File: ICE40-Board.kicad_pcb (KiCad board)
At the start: 4 copper layers, 134.4 x 58 mm, 82 parts, among them SW1 SW_Push, U1 ADP1712AUJZ-3.3, U10 FT4222HQ, U11 74LS125, U12 74LS126, U2 ADP1712AUJZ-2.5, U3 ADP1712AUJZ-1.2, U4 Barrel_Jack, U5 W25X20CLSNIG, U6 USB_C_Receptacle_USB2.0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

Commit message: Minor changed
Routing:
- net Net-(U7-Pad42): track 33.5 -> 31.1 mm
- net Net-(U7-Pad43): track 32.1 -> 30.0 mm
- net Net-(U7-Pad44): track 39.0 -> 37.3 mm
- net Net-(U7-Pad45): track 43.6 -> 42.3 mm
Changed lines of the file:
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@@
   (gr_line (start 22.987 74.676) (end 152.908 74.676) (layer "Edge.Cuts") (width 0.1))
   (gr_arc (start 20.701 18.796) (mid 21.333356 17.269356) (end 22.86 16.637) (layer "Edge.Cuts") (width 0.1))
-  (segment (start 101.9355 40.4675) (end 116.205 40.4675) (width 0.2) (layer "F.Cu") (net 1))
-  (segment (start 98.552 39.624) (end 101.092 39.624) (width 0.2) (layer "F.Cu") (net 1))
-  (segment (start 94.234 46.99) (end 97.79 43.434) (width 0.2) (layer "F.Cu") (net 1))
-  (segment (start 94.291006 51.308) (end 95.14152 50.457486) (width 0.2) (layer "F.Cu") (net 1))
-  (segment (start 89.916 56.896) (end 90.678 56.896) (width 0.2) (layer "F.Cu") (net 1))
-  (segment (start 94.234 48.006) (end 94.234 46.99) (width 0.2) (layer "F.Cu") (net 1))
-  (segment (start 95.14152 48.91352) (end 94.234 48.006) (width 0.2) (layer "F.Cu") (net 1))
-  (segment (start 97.79 40.386) (end 98.552 39.624) (width 0.2) (layer "F.Cu") (net 1))
+  (segment (start 97.917 43.688) (end 97.917 41.402) (width 0.2) (layer "F.Cu") (net 1))
+  (segment (start 90.678 56.896) (end 91.44848 56.12552) (width 0.2) (layer "F.Cu") (net 1))
   (segment (start 92.964 51.308) (end 94.291006 51.308) (width 0.2) (layer "F.Cu") (net 1))
   (segment (start 95.14152 50.457486) (end 95.14152 48.91352) (width 0.2) (layer "F.Cu") (net 1))
+  (segment (start 91.44848 52.82352) (end 92.964 51.308) (width 0.2) (layer "F.Cu") (net 1))
+  (segment (start 89.535 56.515) (end 89.916 56.896) (width 0.2) (layer "F.Cu") (net 1))
+  (segment (start 115.356349 40.386) (end 115.437849 40.4675) (width 0.2) (layer "F.Cu") (net 1))
+  (segment (start 94.234 48.006) (end 94.234 47.371) (width 0.2) (layer "F.Cu") (net 1))
+  (segment (start 97.917 41.402) (end 98.933 40.386) (width 0.2) (layer "F.Cu") (net 1))
+  (segment (start 115.437849 40.4675) (end 116.205 40.4675) (width 0.2) (layer "F.Cu") (net 1))
+  (segment (start 94.291006 51.308) (end 95.14152 50.457486) (width 0.2) (layer "F.Cu") (net 1))
   (segment (start 89.535 54.291) (end 89.535 56.515) (width 0.2) (layer "F.Cu") (net 1))
-  (segment (start 89.535 56.515) (end 89.916 56.896) (width 0.2) (layer "F.Cu") (net 1))
-  (segment (start 90.678 56.896) (end 91.44848 56.12552) (width 0.2) (layer "F.Cu") (net 1))
-  (segment (start 91.44848 52.82352) (end 92.964 51.308) (width 0.2) (layer "F.Cu") (net 1))
+  (segment (start 98.933 40.386) (end 115.356349 40.386) (width 0.2) (layer "F.Cu") (net 1))
+  (segment (start 94.234 47.371) (end 97.917 43.688) (width 0.2) (layer "F.Cu") (net 1))
   (segment (start 91.44848 56.12552) (end 91.44848 52.82352) (width 0.2) (layer "F.Cu") (net 1))
-  (segment (start 97.79 43.434) (end 97.79 40.386) (width 0.2) (layer "F.Cu") (net 1))
-  (segment (start 101.092 39.624) (end 101.9355 40.4675) (width 0.2) (layer "F.Cu") (net 1))
-  (segment (start 97.17352 40.24048) (end 98.806 38.608) (width 0.2) (layer "F.Cu") (net 2))
-  (segment (start 102.845488 39.9675) (end 116.205 39.9675) (width 0.2) (layer "F.Cu") (net 2))
+  (segment (start 89.916 56.896) (end 90.678 56.896) (width 0.2) (layer "F.Cu") (net 1))
+  (segment (start 95.14152 48.91352) (end 94.234 48.006) (width 0.2) (layer "F.Cu") (net 1))
+  (segment (start 97.17352 41.25648) (end 98.4625 39.9675) (width 0.2) (layer "F.Cu") (net 2))
+  (segment (start 90.805 54.291) (end 90.805 52.197) (width 0.2) (layer "F.Cu") (net 2))
   (segment (start 94.742 50.292) (end 94.742 49.127283) (width 0.2) (layer "F.Cu") (net 2))
-  (segment (start 101.485988 38.608) (end 102.845488 39.9675) (width 0.2) (layer "F.Cu") (net 2))
-  (segment (start 93.74452 48.129803) (end 93.74452 46.802989) (width 0.2) (layer "F.Cu") (net 2))
-  (segment (start 98.806 38.608) (end 101.485988 38.608) (width 0.2) (layer "F.Cu") (net 2))
   (segment (start 94.234 50.8) (end 94.742 50.292) (width 0.2) (layer "F.Cu") (net 2))
-  (segment (start 93.74452 46.802989) (end 97.17352 43.373989) (width 0.2) (layer "F.Cu") (net 2))
+  (segment (start 93.74452 47.09848) (end 97.17352 43.66948) (width 0.2) (layer "F.Cu") (net 2))
+  (segment (start 90.805 52.197) (end 92.202 50.8) (width 0.2) (layer "F.Cu") (net 2))
+  (segment (start 93.74452 48.129803) (end 93.74452 47.09848) (width 0.2) (layer "F.Cu") (net 2))
+  (segment (start 92.202 50.8) (end 94.234 50.8) (width 0.2) (layer "F.Cu") (net 2))
+  (segment (start 98.4625 39.9675) (end 116.205 39.9675) (width 0.2) (layer "F.Cu") (net 2))
+  (segment (start 97.17352 43.66948) (end 97.17352 41.25648) (width 0.2) (layer "F.Cu") (net 2))
   (segment (start 94.742 49.127283) (end 93.74452 48.129803) (width 0.2) (layer "F.Cu") (net 2))
-  (segment (start 90.805 54.291) (end 90.805 52.197) (width 0.2) (layer "F.Cu") (net 2))
-  (segment (start 90.805 52.197) (end 92.202 50.8) (width 0.2) (layer "F.Cu") (net 2))
-  (segment (start 92.202 50.8) (end 94.234 50.8) (width 0.2) (layer "F.Cu") (net 2))
-  (segment (start 97.17352 43.373989) (end 97.17352 40.24048) (width 0.2) (layer "F.Cu") (net 2))
   (segment (start 102.7665 56.134) (end 104.648 56.134) (width 0.4) (layer "F.Cu") (net 3))
   (segment (start 126.1175 58.2865) (end 126.1175 55.88) (width 0.2) (layer "F.Cu") (net 3))
@@
   (segment (start 107.442 42.418) (end 107.442 41.0475) (width 0.2) (layer "B.Cu") (net 4))
   (segment (start 107.188 48.387) (end 107.0875 48.2865) (width 0.2) (layer "B.Cu") (net 4))
-  (segment (start 101.288994 37.846) (end 102.910494 39.4675) (width 0.2) (layer "F.Cu") (net 5))
-  (segment (start 98.298 37.846) (end 101.288994 37.846) (width 0.2) (layer "F.Cu") (net 5))
-  (segment (start 96.774 39.37) (end 98.298 37.846) (width 0.2) (layer "F.Cu") (net 5))
-  (segment (start 93.345 46.637503) (end 96.774 43.208503) (width 0.2) (layer "F.Cu") (net 5))
-  (segment (start 102.910494 39.4675) (end 116.205 39.4675) (width 0.2) (layer "F.Cu") (net 5))
-  (segment (start 93.345 49.341) (end 93.345 46.637503) (width 0.2) (layer "F.Cu") (net 5))
-  (segment (start 96.774 43.208503) (end 96.774 39.37) (width 0.2) (layer "F.Cu") (net 5))
-  (segment (start 101.346 37.338) (end 102.9755 38.9675) (width 0.2) (layer "F.Cu") (net 6))
-  (segment (start 92.075 47.117) (end 96.012 43.18) (width 0.2) (layer "F.Cu") (net 6))
-  (segment (start 102.9755 38.9675) (end 116.205 38.9675) (width 0.2) (layer "F.Cu") (net 6))
-  (segment (start 96.012 43.18) (end 96.012 39.116) (width 0.2) (layer "F.Cu") (net 6))
-  (segment (start 92.075 49.341) (end 92.075 47.117) (width 0.2) (layer "F.Cu") (net 6))
-  (segment (start 96.012 39.116) (end 97.79 37.338) (width 0.2) (layer "F.Cu") (net 6))
-  (segment (start 97.79 37.338) (end 101.346 37.338) (width 0.2) (layer "F.Cu") (net 6))
+  (segment (start 93.345 46.355) (end 96.647 43.053) (width 0.2) (layer "F.Cu") (net 5))
+  (segment (start 96.647 43.053) (end 96.647 40.894) (width 0.2) (layer "F.Cu") (net 5))
+  (segment (start 93.345 49.341) (end 93.345 46.355) (width 0.2) (layer "F.Cu") (net 5))
+  (segment (start 96.647 40.894) (end 98.0735 39.4675) (width 0.2) (layer "F.Cu") (net 5))
+  (segment (start 98.0735 39.4675) (end 116.205 39.4675) (width 0.2) (layer "F.Cu") (net 5))
+  (segment (start 92.075 46.736) (end 96.012 42.799) (width 0.2) (layer "F.Cu") (net 6))
+  (segment (start 96.012 42.799) (end 96.012 40.767) (width 0.2) (layer "F.Cu") (net 6))
+  (segment (start 92.075 49.341) (end 92.075 46.736) (width 0.2) (layer "F.Cu") (net 6))
+  (segment (start 96.012 40.767) (end 97.8115 38.9675) (width 0.2) (layer "F.Cu") (net 6))
+  (segment (start 97.8115 38.9675) (end 116.205 38.9675) (width 0.2) (layer "F.Cu") (net 6))
   (segment (start 97.282 36.576) (end 102.698982 36.576) (width 0.2) (layer "F.Cu") (net 7))
   (segment (start 102.698982 36.576) (end 104.590482 38.4675) (width 0.2) (layer "F.Cu") (net 7))

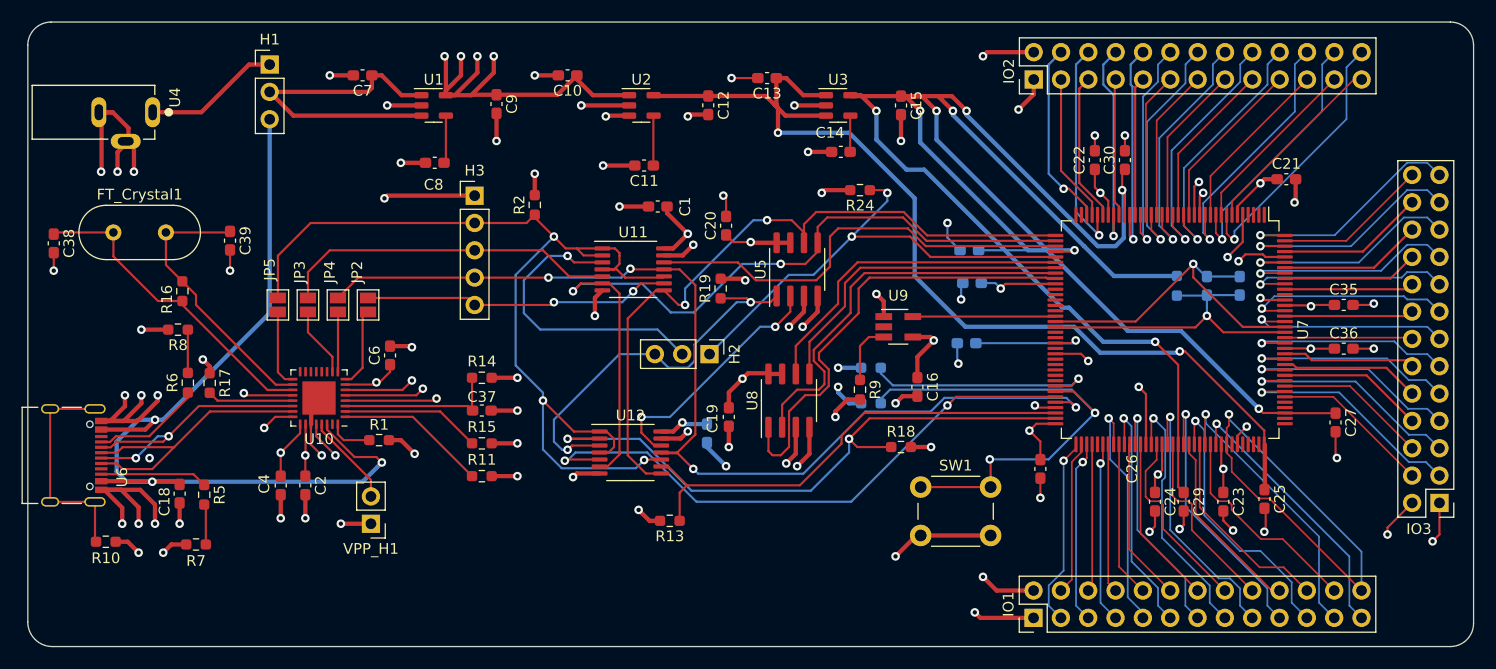
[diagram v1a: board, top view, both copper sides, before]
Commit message: Adjusted component and track clearances
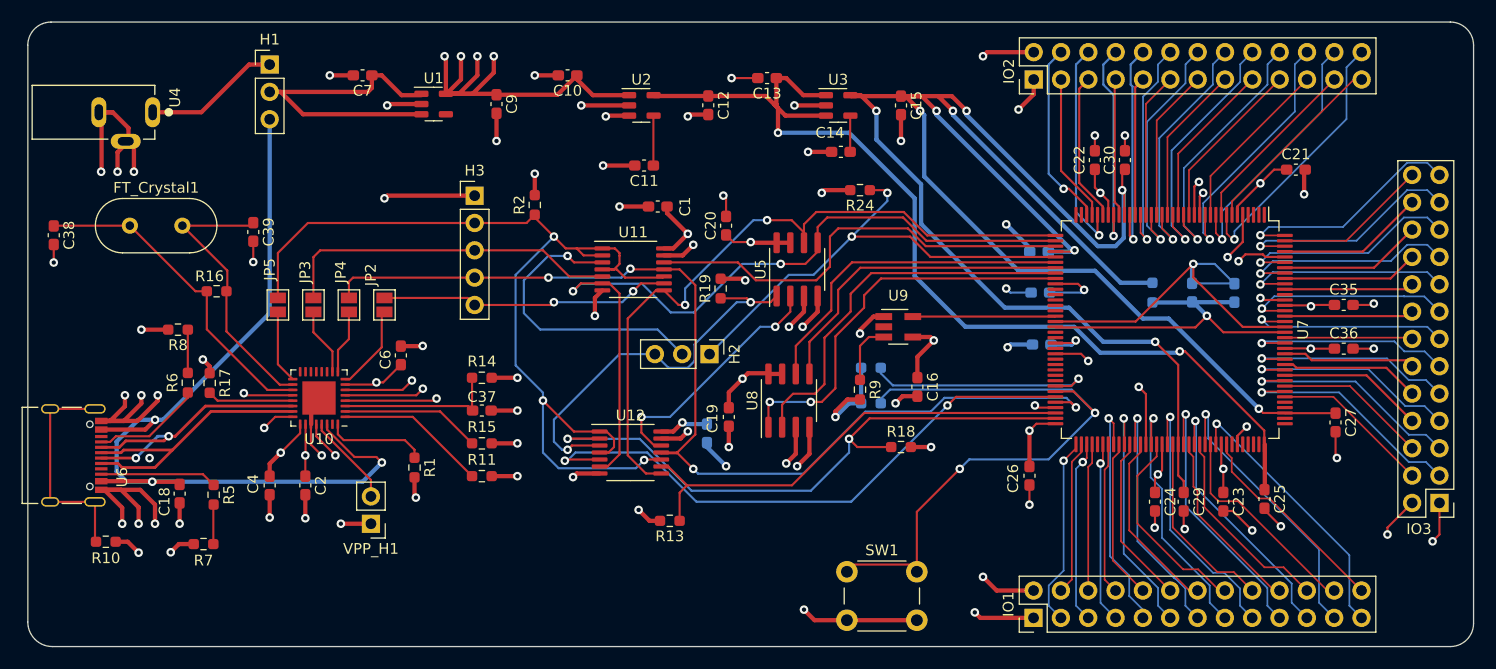
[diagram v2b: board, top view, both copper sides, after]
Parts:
- removed C8: 10nF, Capacitor_SMD:C_0603_1608Metric_Pad1.08x0.95mm_HandSolder
- IO3: value Conn_02x13_Row_Letter_Last -> Conn_02x09_Row_Letter_Last
- U1: value ADP1712AUJZ-3.3 -> ADP122AUJZ-3.3-R7
- moved SW1 10.4 mm to (96.8, 67.7)
- moved C31 6.99 mm to (114.9, 46.6)
- moved C28 6.48 mm to (114.7, 38.0)
- moved C32 6.41 mm to (114.8, 41.8)
- moved R1 4.16 mm to (56.6, 58.0), turned to -90 degrees
- moved R16 3.19 mm to (38.3, 41.7), turned to 0 degrees
- moved R12 2.36 mm to (125.2, 41.8)
- moved C39 2.30 mm to (41.7, 36.1)
- moved FT_Crystal1 1.66 mm to (30.2, 35.6)
- moved JP2 1.52 mm to (53.8, 42.9)
- moved C34 1.52 mm to (128.9, 41.8)
- moved C21 1.26 mm to (138.6, 30.4)
- moved C26 1.20 mm to (113.8, 58.8)
- moved C4 1.03 mm to (43.2, 59.7)
- moved JP4 1.02 mm to (50.5, 42.9)
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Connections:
- U1 pad 4: Net-(C8-Pad1) -> unconnected-(U1-Pad4)
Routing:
- net /12b: track 43.7 -> 19.4 mm, vias 1 -> 0
- net Net-(R4-Pad1): track 46.8 -> 58.5 mm
- net +1V2: track 213.2 -> 207.2 mm
- net /GND_PLL1: track 31.5 -> 37.1 mm
- net Net-(R1-Pad1): track 4.08 -> 9.39 mm
- net Net-(U7-Pad45): track 42.3 -> 37.2 mm, vias 0 -> 2
- net Net-(C8-Pad1): track 4.46 -> 0.00 mm
- net GND: track 251.2 -> 253.3 mm, vias 78 -> 77
- net +3V3: track 206.7 -> 204.7 mm, vias 42 -> 40
- net /VCC_PLL1: track 30.1 -> 31.9 mm
- net /SCK_EXT: track 28.6 -> 27.1 mm
- net /6b: track 15.8 -> 17.1 mm
- net /7b: track 17.6 -> 18.8 mm
- net Net-(U7-Pad44): track 37.3 -> 36.1 mm
- net /10a: track 25.9 -> 24.8 mm
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
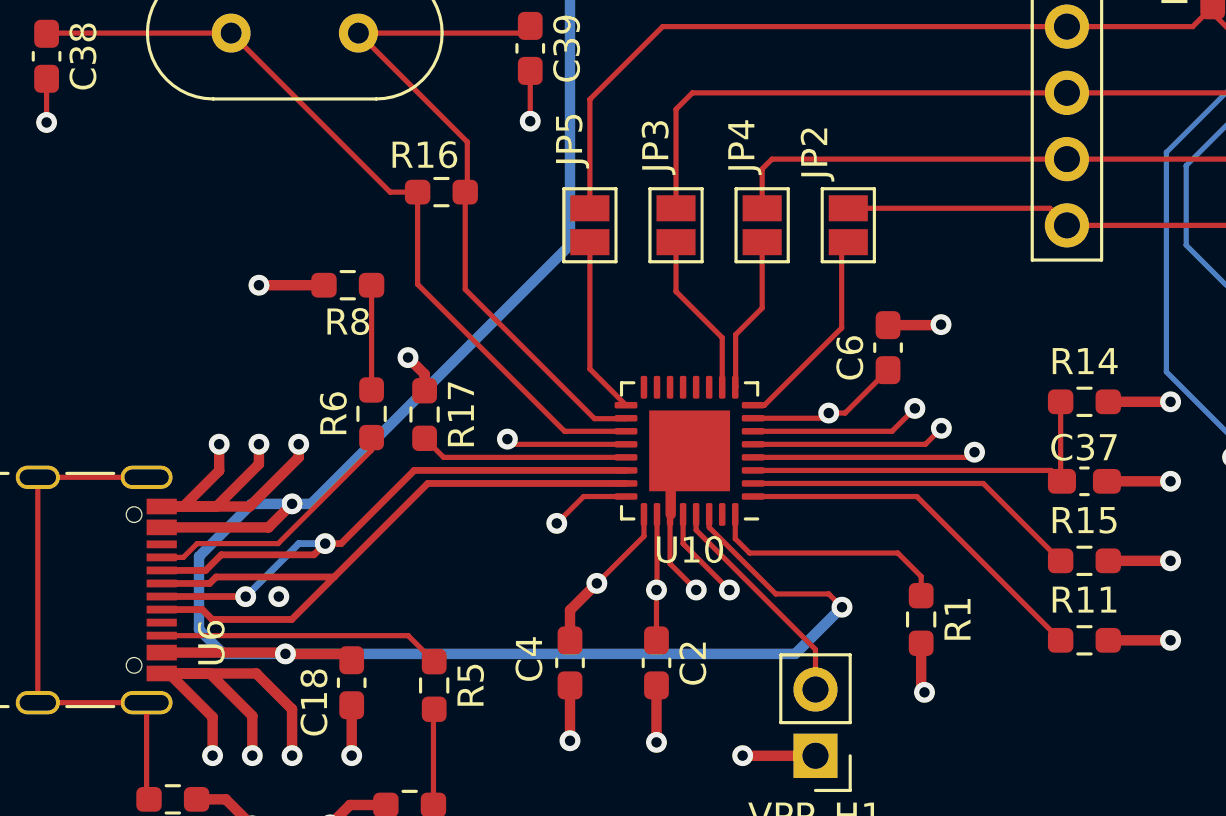
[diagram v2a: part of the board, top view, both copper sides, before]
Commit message: Impedance controlled USB routing
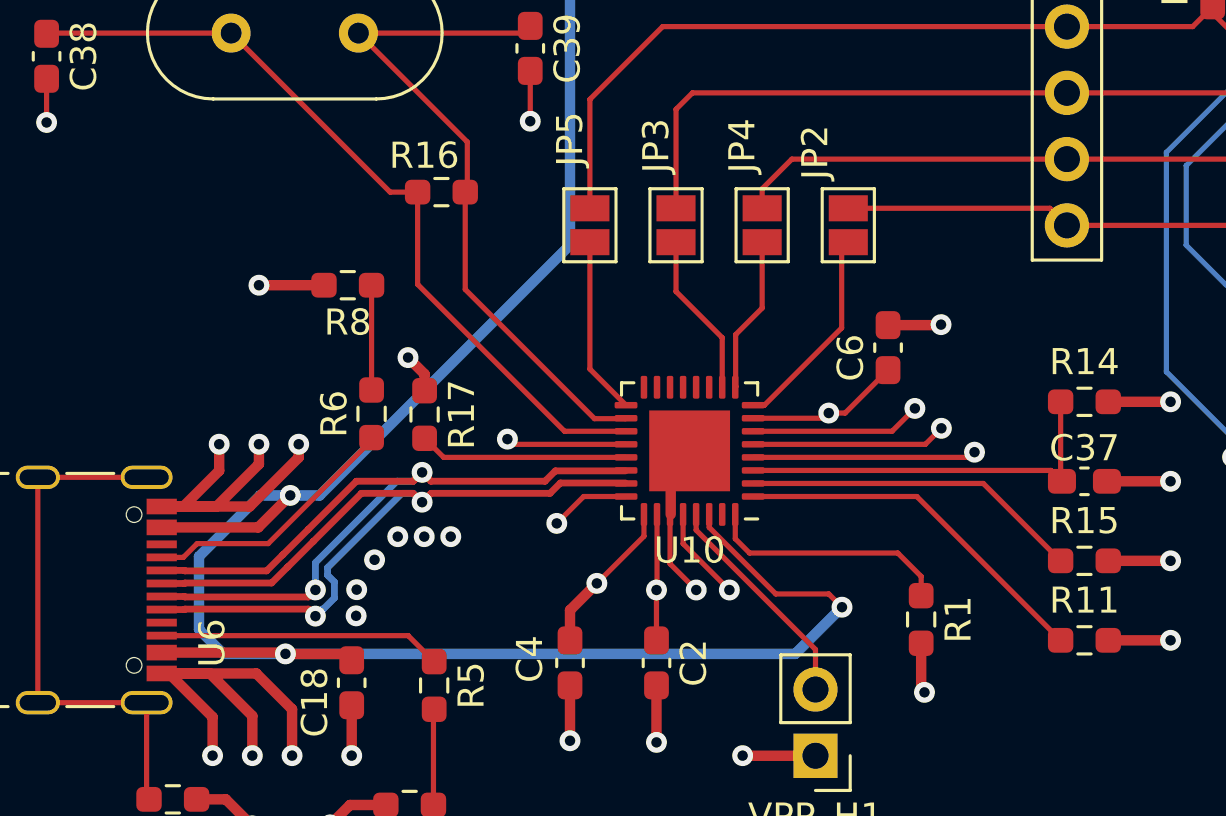
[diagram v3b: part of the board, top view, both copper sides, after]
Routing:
- net D+: track 26.8 -> 32.9 mm, vias 0 -> 2
- net D-: track 26.5 -> 32.2 mm
- net GND: vias 77 -> 82

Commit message: Added ground vias for better signal integrity, added silkscreen text, added reset button for MCU
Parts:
- added R20: 10k, Resistor_SMD:R_0603_1608Metric_Pad0.98x0.95mm_HandSolder, F.Cu at (72.0, 68.6)
- added SW2: SW_Push, Button_Switch_THT:SW_PUSH_6mm, F.Cu at (79.0, 67.7)
- R3, R4: moved to F.Cu
- moved R4 17.7 mm to (91.1, 67.8), turned to -90 degrees
- moved R3 10.3 mm to (109.3, 48.9)
- moved VPP_H1 3.92 mm to (52.6, 67.2)
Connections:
- IO3 pad 1: +3V3 -> GND
- IO3 pad 2: GND -> +3V3
- U7 pad 110: unconnected-(U7-Pad110) -> /MCU_RESET
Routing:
- net /MCU_RESET: track 0.00 -> 73.2 mm, vias 0 -> 2
- net Net-(R3-Pad1): track 22.0 -> 5.86 mm, vias 1 -> 0
- net Net-(R4-Pad1): track 58.5 -> 42.4 mm
- net GND: track 253.3 -> 265.9 mm, vias 82 -> 123
- net Net-(U10-Pad29): track 8.61 -> 12.5 mm
- net +3V3: track 204.7 -> 207.2 mm, vias 40 -> 43
- net /SS_EXT: track 94.7 -> 93.4 mm
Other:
- board text added: "12MHz"
- board text added: "6.5V In"
- board text added: "FPGA"
- board text added: "FPGA Reset"
- board text added: "MCU"
- board text added: "MCU Reset"
- board text added: "MISO"
- board text added: "MOSI"
- board text added: "SCK"
- board text added: "SS"
- board text added: "V_EXT"
- board text added: "V_USB"
- board text added: "gnd"
